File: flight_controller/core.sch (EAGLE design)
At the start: 115 parts, among them J1 M02, J10 M02, J11 M02, J12 M02, J13 M02, J14 M02, J15 M02, J16 M03, J17 M03, J18 M04, J19 M04, J2 M02, J20 M03, J21 M04, J3 M02, J4 M03, J5 M02, J6 M02, J7 M02, J8 M02, J9 M03, Q1 EM6K1, Q2 EM6K1, Q3 EM6K1, Q4 EM6K1, Q5 EM6K1, Q6 EM6K1, Q7 MOSFET-PCHANNEL-AON6407, U1 STM32F405, U2 MEAS-MS5611, U3 MPU-9250-QFN-24-NP, U4 MIC5219 3.3V, U5 USD-SOCKETNEW, Y1 16MHz

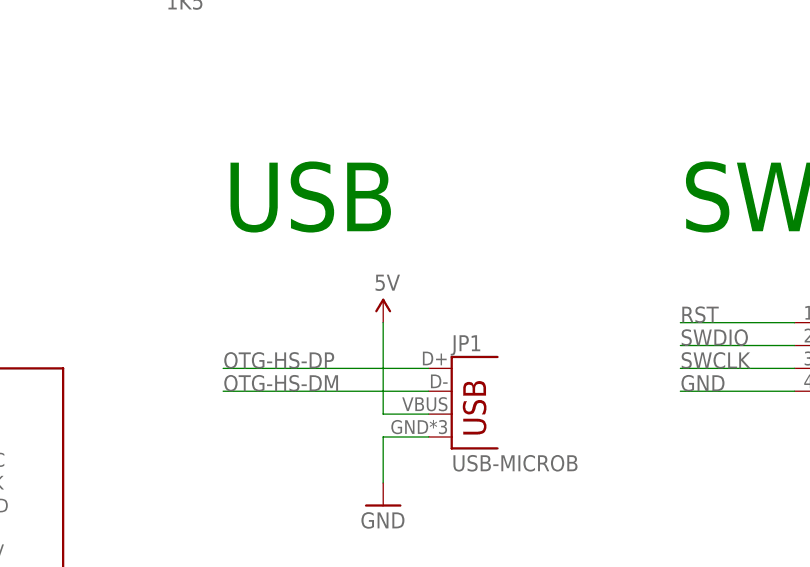
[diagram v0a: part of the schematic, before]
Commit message: Move USB 5V to VIN.
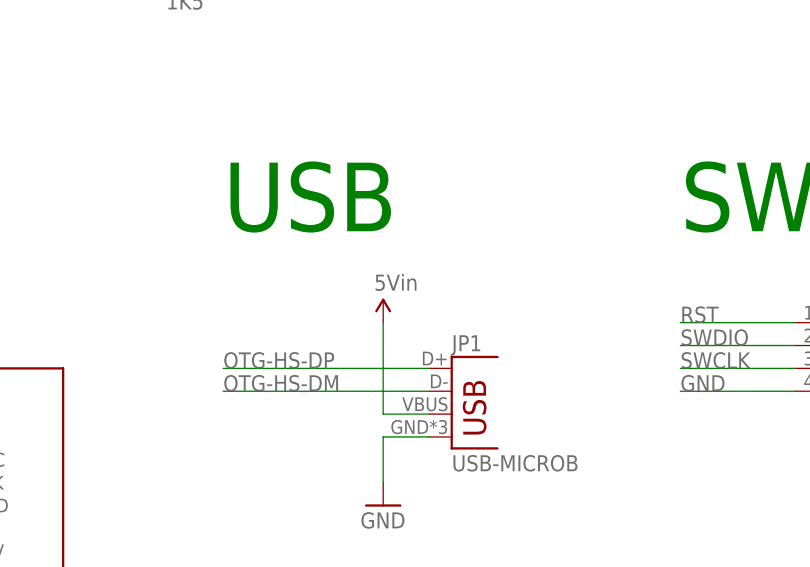
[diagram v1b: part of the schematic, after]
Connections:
- net 5V: no longer JP1.VBUS
- net VIN: now also JP1.VBUS
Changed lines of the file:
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@@
 <part name="JP1" library="SparkFun-Connectors" deviceset="USB" device="-MICROB"/>
 <part name="GND10" library="SparkFun-Aesthetics" deviceset="GND" device=""/>
-<part name="SUPPLY12" library="SparkFun-Aesthetics" deviceset="5V" device=""/>
 <part name="SUPPLY15" library="SparkFun-Aesthetics" deviceset="3.3V" device=""/>
 <part name="GND11" library="SparkFun-Aesthetics" deviceset="GND" device=""/>
@@
 <part name="J21" library="OSURC_Connectors" deviceset="M04" device=""/>
 <part name="J2" library="OSURC_Connectors" deviceset="M02" device=""/>
+<part name="SUPPLY1" library="SparkFun-Aesthetics" deviceset="VIN" device="" value="5Vin"/>
 </parts>
 <sheets>
@@
 <instance part="JP1" gate="G$1" x="106.68" y="-586.74"/>
 <instance part="GND10" gate="1" x="99.06" y="-594.36"/>
-<instance part="SUPPLY12" gate="G$1" x="99.06" y="-574.04"/>
 <instance part="SUPPLY15" gate="G$1" x="40.64" y="-574.04"/>
 <instance part="GND11" gate="1" x="40.64" y="-622.3"/>
@@
 <instance part="J21" gate="G$1" x="149.86" y="-579.12"/>
 <instance part="J2" gate="G$1" x="78.74" y="-416.56"/>
+<instance part="SUPPLY1" gate="G$1" x="99.06" y="-574.04"/>
 </instances>
 <busses>
@@
 <wire x1="139.7" y1="228.6" x2="132.08" y2="228.6" width="0.1524" layer="91"/>
 <label x="132.08" y="228.6" size="1.778" layer="95"/>
-</segment>
-<segment>
-<pinref part="JP1" gate="G$1" pin="VBUS"/>
-<wire x1="104.14" y1="-584.2" x2="99.06" y2="-584.2" width="0.1524" layer="91"/>
-<wire x1="99.06" y1="-584.2" x2="99.06" y2="-574.04" width="0.1524" layer="91"/>
-<pinref part="SUPPLY12" gate="G$1" pin="5V"/>
 </segment>
 <segment>
@@
 <pinref part="D1" gate="G$1" pin="2"/>
 </segment>
-</net>
+<segment>
+<pinref part="JP1" gate="G$1" pin="VBUS"/>
+<wire x1="104.14" y1="-584.2" x2="99.06" y2="-584.2" width="0.1524" layer="91"/>
+<wire x1="99.06" y1="-584.2" x2="99.06" y2="-574.04" width="0.1524" layer="91"/>
+<pinref part="SUPPLY1" gate="G$1" pin="VIN"/>
+</segment>
+</net>

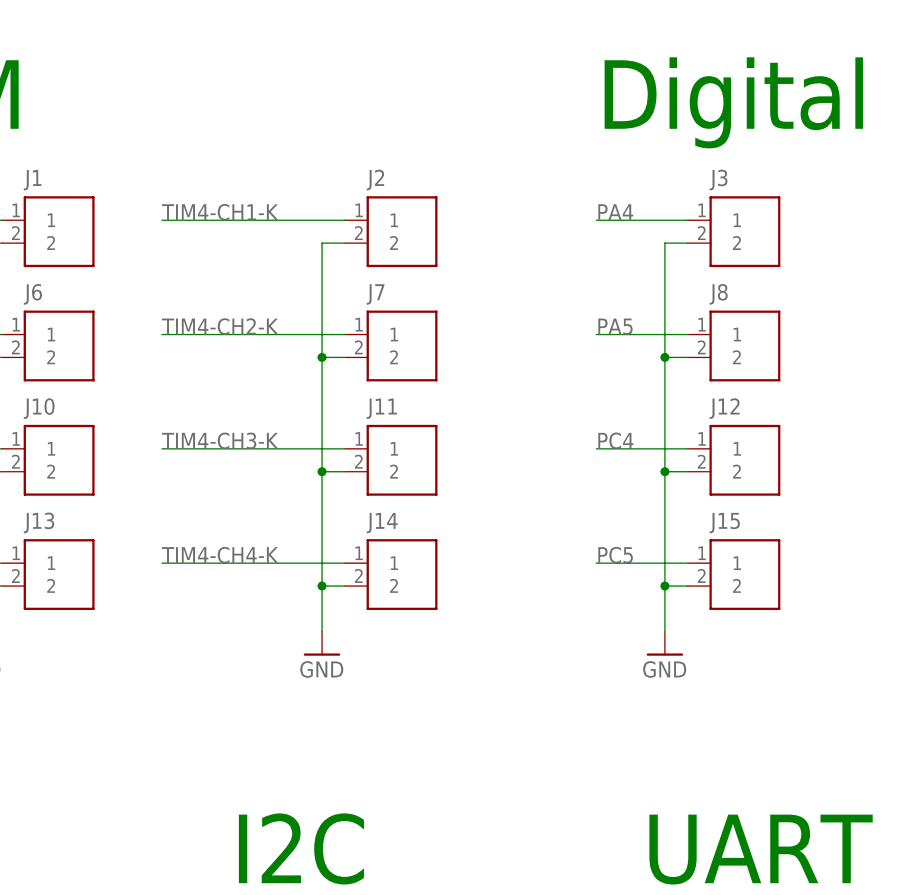
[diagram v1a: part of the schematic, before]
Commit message: Make last two PWM outputs 5V powered (for servos).
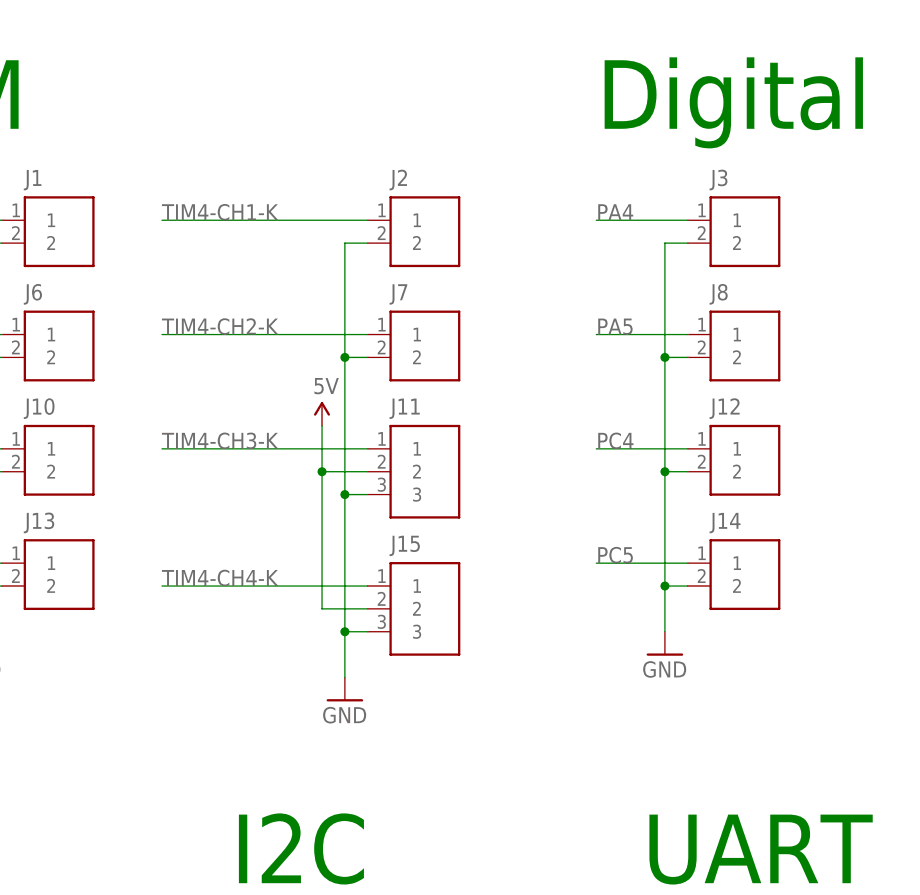
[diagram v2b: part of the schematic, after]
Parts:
- J11, J15: value M02 -> M03; device OSURC_Connectors:M02 -> OSURC_Connectors:M03
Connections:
- net 5V: now also J11.2, J15.2
- net GND: now also J11.3, J15.3; no longer J11.2, J15.2
- net PC5: now also J14.1; no longer J15.1
- net TIM4-CH4-K: now also J15.1; no longer J14.1
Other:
- moved on the sheet: J14, J2, J7
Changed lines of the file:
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@@
 <part name="J13" library="OSURC_Connectors" deviceset="M02" device=""/>
 <part name="J7" library="OSURC_Connectors" deviceset="M02" device=""/>
-<part name="J11" library="OSURC_Connectors" deviceset="M02" device=""/>
-<part name="J14" library="OSURC_Connectors" deviceset="M02" device=""/>
 <part name="J3" library="OSURC_Connectors" deviceset="M02" device=""/>
 <part name="J8" library="OSURC_Connectors" deviceset="M02" device=""/>
 <part name="J12" library="OSURC_Connectors" deviceset="M02" device=""/>
-<part name="J15" library="OSURC_Connectors" deviceset="M02" device=""/>
+<part name="J14" library="OSURC_Connectors" deviceset="M02" device=""/>
 <part name="J5" library="OSURC_Connectors" deviceset="M02" device=""/>
 <part name="J4" library="OSURC_Connectors" deviceset="M03" device=""/>
@@
 <part name="J2" library="OSURC_Connectors" deviceset="M02" device=""/>
 <part name="SUPPLY1" library="SparkFun-Aesthetics" deviceset="VIN" device="" value="5Vin"/>
+<part name="J11" library="OSURC_Connectors" deviceset="M03" device=""/>
+<part name="J15" library="OSURC_Connectors" deviceset="M03" device=""/>
+<part name="SUPPLY12" library="SparkFun-Aesthetics" deviceset="5V" device=""/>
 </parts>
 <sheets>
@@
 <instance part="SUPPLY4" gate="G$1" x="190.5" y="-414.02"/>
 <instance part="GND4" gate="1" x="33.02" y="-462.28"/>
-<instance part="GND5" gate="1" x="71.12" y="-462.28"/>
+<instance part="GND5" gate="1" x="73.66" y="-467.36"/>
 <instance part="GND7" gate="1" x="127" y="-528.32"/>
 <instance part="U5" gate="G$1" x="53.34" y="-594.36"/>
@@
 <instance part="J10" gate="G$1" x="40.64" y="-441.96"/>
 <instance part="J13" gate="G$1" x="40.64" y="-454.66"/>
-<instance part="J7" gate="G$1" x="78.74" y="-429.26"/>
-<instance part="J11" gate="G$1" x="78.74" y="-441.96"/>
-<instance part="J14" gate="G$1" x="78.74" y="-454.66"/>
+<instance part="J7" gate="G$1" x="81.28" y="-429.26"/>
 <instance part="J3" gate="G$1" x="116.84" y="-416.56"/>
 <instance part="J8" gate="G$1" x="116.84" y="-429.26"/>
 <instance part="J12" gate="G$1" x="116.84" y="-441.96"/>
-<instance part="J15" gate="G$1" x="116.84" y="-454.66"/>
+<instance part="J14" gate="G$1" x="116.84" y="-454.66"/>
 <instance part="J5" gate="G$1" x="358.14" y="-421.64"/>
 <instance part="J4" gate="G$1" x="200.66" y="-421.64"/>
@@
 <instance part="J19" gate="G$1" x="175.26" y="-508"/>
 <instance part="J21" gate="G$1" x="149.86" y="-579.12"/>
-<instance part="J2" gate="G$1" x="78.74" y="-416.56"/>
+<instance part="J2" gate="G$1" x="81.28" y="-416.56"/>
 <instance part="SUPPLY1" gate="G$1" x="99.06" y="-574.04"/>
+<instance part="J11" gate="G$1" x="81.28" y="-441.96"/>
+<instance part="J15" gate="G$1" x="81.28" y="-457.2"/>
+<instance part="SUPPLY12" gate="G$1" x="71.12" y="-436.88"/>
 </instances>
 <busses>
@@
 </segment>
 <segment>
-<wire x1="73.66" y1="-416.56" x2="71.12" y2="-416.56" width="0.1524" layer="91"/>
-<wire x1="73.66" y1="-454.66" x2="71.12" y2="-454.66" width="0.1524" layer="91"/>
-<wire x1="71.12" y1="-416.56" x2="71.12" y2="-429.26" width="0.1524" layer="91"/>
-<wire x1="71.12" y1="-429.26" x2="71.12" y2="-441.96" width="0.1524" layer="91"/>
-<wire x1="71.12" y1="-441.96" x2="71.12" y2="-454.66" width="0.1524" layer="91"/>
-<wire x1="73.66" y1="-429.26" x2="71.12" y2="-429.26" width="0.1524" layer="91"/>
-<junction x="71.12" y="-429.26"/>
-<wire x1="73.66" y1="-441.96" x2="71.12" y2="-441.96" width="0.1524" layer="91"/>
-<junction x="71.12" y="-441.96"/>
+<wire x1="76.2" y1="-416.56" x2="73.66" y2="-416.56" width="0.1524" layer="91"/>
+<wire x1="76.2" y1="-459.74" x2="73.66" y2="-459.74" width="0.1524" layer="91"/>
+<wire x1="73.66" y1="-416.56" x2="73.66" y2="-429.26" width="0.1524" layer="91"/>
+<wire x1="73.66" y1="-429.26" x2="73.66" y2="-444.5" width="0.1524" layer="91"/>
+<wire x1="73.66" y1="-444.5" x2="73.66" y2="-459.74" width="0.1524" layer="91"/>
+<wire x1="76.2" y1="-429.26" x2="73.66" y2="-429.26" width="0.1524" layer="91"/>
+<junction x="73.66" y="-429.26"/>
+<wire x1="76.2" y1="-444.5" x2="73.66" y2="-444.5" width="0.1524" layer="91"/>
+<junction x="73.66" y="-444.5"/>
 <pinref part="GND5" gate="1" pin="GND"/>
-<wire x1="71.12" y1="-454.66" x2="71.12" y2="-459.74" width="0.1524" layer="91"/>
-<junction x="71.12" y="-454.66"/>
+<wire x1="73.66" y1="-459.74" x2="73.66" y2="-464.82" width="0.1524" layer="91"/>
+<junction x="73.66" y="-459.74"/>
 <pinref part="J7" gate="G$1" pin="2"/>
-<pinref part="J11" gate="G$1" pin="2"/>
-<pinref part="J14" gate="G$1" pin="2"/>
 <pinref part="J2" gate="G$1" pin="2"/>
+<pinref part="J11" gate="G$1" pin="3"/>
+<pinref part="J15" gate="G$1" pin="3"/>
 </segment>
 <segment>
@@
 <pinref part="J8" gate="G$1" pin="2"/>
 <pinref part="J12" gate="G$1" pin="2"/>
-<pinref part="J15" gate="G$1" pin="2"/>
+<pinref part="J14" gate="G$1" pin="2"/>
 </segment>
 </net>
@@
 <pinref part="J4" gate="G$1" pin="2"/>
 <pinref part="J9" gate="G$1" pin="2"/>
+</segment>
+<segment>
+<pinref part="J11" gate="G$1" pin="2"/>
+<wire x1="76.2" y1="-441.96" x2="71.12" y2="-441.96" width="0.1524" layer="91"/>
+<wire x1="71.12" y1="-441.96" x2="71.12" y2="-436.88" width="0.1524" layer="91"/>
+<pinref part="J15" gate="G$1" pin="2"/>
+<wire x1="76.2" y1="-457.2" x2="71.12" y2="-457.2" width="0.1524" layer="91"/>
+<wire x1="71.12" y1="-457.2" x2="71.12" y2="-441.96" width="0.1524" layer="91"/>
+<junction x="71.12" y="-441.96"/>
+<pinref part="SUPPLY12" gate="G$1" pin="5V"/>
 </segment>
 </net>
@@
 <wire x1="111.76" y1="-452.12" x2="101.6" y2="-452.12" width="0.1524" layer="91"/>
 <label x="101.6" y="-452.12" size="1.778" layer="95"/>
-<pinref part="J15" gate="G$1" pin="1"/>
+<pinref part="J14" gate="G$1" pin="1"/>
 </segment>
 </net>
@@
 <net name="TIM4-CH1-K" class="0">
 <segment>
-<wire x1="73.66" y1="-414.02" x2="53.34" y2="-414.02" width="0.1524" layer="91"/>
+<wire x1="76.2" y1="-414.02" x2="53.34" y2="-414.02" width="0.1524" layer="91"/>
 <label x="53.34" y="-414.02" size="1.778" layer="95"/>
 <pinref part="J2" gate="G$1" pin="1"/>
@@
 <net name="TIM4-CH2-K" class="0">
 <segment>
-<wire x1="73.66" y1="-426.72" x2="53.34" y2="-426.72" width="0.1524" layer="91"/>
+<wire x1="76.2" y1="-426.72" x2="53.34" y2="-426.72" width="0.1524" layer="91"/>
 <label x="53.34" y="-426.72" size="1.778" layer="95"/>
 <pinref part="J7" gate="G$1" pin="1"/>
@@
 <net name="TIM4-CH3-K" class="0">
 <segment>
-<wire x1="73.66" y1="-439.42" x2="53.34" y2="-439.42" width="0.1524" layer="91"/>
+<wire x1="76.2" y1="-439.42" x2="53.34" y2="-439.42" width="0.1524" layer="91"/>
 <label x="53.34" y="-439.42" size="1.778" layer="95"/>
 <pinref part="J11" gate="G$1" pin="1"/>
@@
 <net name="TIM4-CH4-K" class="0">
 <segment>
-<wire x1="73.66" y1="-452.12" x2="53.34" y2="-452.12" width="0.1524" layer="91"/>
-<label x="53.34" y="-452.12" size="1.778" layer="95"/>
-<pinref part="J14" gate="G$1" pin="1"/>
-</segment>
-<segment>
+<wire x1="76.2" y1="-454.66" x2="53.34" y2="-454.66" width="0.1524" layer="91"/>
+<label x="53.34" y="-454.66" size="1.778" layer="95"/>
+<pinref part="J15" gate="G$1" pin="1"/>
+</segment>
+<segment>

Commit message: Component placement almost done, routing halfway done.
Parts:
- added S2, S3, S4, S5: STANDOFF_ELECTRICAL-#4, OSURC_Electromechanical:STANDOFF_ELECTRICAL-#4
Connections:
- net N$12 renamed STSB1+
- net N$15 renamed STSR2+
- net N$16 renamed STSG2+
- net N$19 renamed STSB2+
- net N$5 renamed STSB-
- net N$6 renamed STSG-
- net N$7 renamed STSR-
- net N$8 renamed STSR1+
- net N$9 renamed STSG1+
- removed net OTG-HS-ID: U1.GPIO.PB12
- net GND: now also S2.P$1, S3.P$1, S4.P$1, S5.P$1
- net USD-CD: now also U1.GPIO.PB12
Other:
- note added: "Standoffs"
- note added: "TODO: C15 unused"
- note removed: "TODO: B12 and C15 unused"
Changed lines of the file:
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@@
 <part name="J15" library="OSURC_Connectors" deviceset="M03" device=""/>
 <part name="SUPPLY12" library="SparkFun-Aesthetics" deviceset="5V" device=""/>
+<part name="S2" library="OSURC_Electromechanical" deviceset="STANDOFF_ELECTRICAL" device="-#4"/>
+<part name="S3" library="OSURC_Electromechanical" deviceset="STANDOFF_ELECTRICAL" device="-#4"/>
+<part name="S4" library="OSURC_Electromechanical" deviceset="STANDOFF_ELECTRICAL" device="-#4"/>
+<part name="S5" library="OSURC_Electromechanical" deviceset="STANDOFF_ELECTRICAL" device="-#4"/>
+<part name="GND6" library="SparkFun-Aesthetics" deviceset="GND" device=""/>
 </parts>
 <sheets>
@@
 <text x="33.02" y="-261.62" size="3.81" layer="91">VDDIO</text>
 <text x="101.6" y="-403.86" size="7.62" layer="91">Digital</text>
-<text x="15.24" y="152.4" size="1.778" layer="98">TODO: B12 and C15 unused</text>
+<text x="15.24" y="152.4" size="1.778" layer="98">TODO: C15 unused</text>
 <text x="15.24" y="-645.16" size="1.778" layer="98">TODO: pullups on data lines?</text>
 <text x="223.52" y="-403.86" size="7.62" layer="91">Test</text>
+<text x="347.98" y="-563.88" size="7.62" layer="91">Standoffs</text>
 </plain>
 <instances>
@@
 <instance part="J15" gate="G$1" x="81.28" y="-457.2"/>
 <instance part="SUPPLY12" gate="G$1" x="71.12" y="-436.88"/>
+<instance part="S2" gate="G$1" x="353.06" y="-576.58"/>
+<instance part="S3" gate="G$1" x="353.06" y="-591.82"/>
+<instance part="S4" gate="G$1" x="353.06" y="-607.06"/>
+<instance part="S5" gate="G$1" x="353.06" y="-622.3"/>
+<instance part="GND6" gate="1" x="363.22" y="-629.92"/>
 </instances>
 <busses>
@@
 <pinref part="J12" gate="G$1" pin="2"/>
 <pinref part="J14" gate="G$1" pin="2"/>
+</segment>
+<segment>
+<pinref part="S2" gate="G$1" pin="P$1"/>
+<wire x1="360.68" y1="-576.58" x2="363.22" y2="-576.58" width="0.1524" layer="91"/>
+<wire x1="363.22" y1="-576.58" x2="363.22" y2="-591.82" width="0.1524" layer="91"/>
+<pinref part="S3" gate="G$1" pin="P$1"/>
+<wire x1="363.22" y1="-591.82" x2="363.22" y2="-607.06" width="0.1524" layer="91"/>
+<wire x1="363.22" y1="-607.06" x2="363.22" y2="-622.3" width="0.1524" layer="91"/>
+<wire x1="363.22" y1="-622.3" x2="363.22" y2="-627.38" width="0.1524" layer="91"/>
+<wire x1="360.68" y1="-591.82" x2="363.22" y2="-591.82" width="0.1524" layer="91"/>
+<pinref part="S4" gate="G$1" pin="P$1"/>
+<wire x1="360.68" y1="-607.06" x2="363.22" y2="-607.06" width="0.1524" layer="91"/>
+<pinref part="S5" gate="G$1" pin="P$1"/>
+<wire x1="360.68" y1="-622.3" x2="363.22" y2="-622.3" width="0.1524" layer="91"/>
+<pinref part="GND6" gate="1" pin="GND"/>
+<junction x="363.22" y="-591.82"/>
+<junction x="363.22" y="-607.06"/>
+<junction x="363.22" y="-622.3"/>
 </segment>
 </net>
@@
 </segment>
 </net>
-<net name="OTG-HS-ID" class="0">
-<segment>
-<wire x1="53.34" y1="170.18" x2="30.48" y2="170.18" width="0.1524" layer="91"/>
-<label x="30.48" y="170.18" size="1.778" layer="95"/>
-<pinref part="U1" gate=".GPIO" pin="PB12"/>
-</segment>
-</net>
 <net name="OTG-HS-DM" class="0">
 <segment>
@@
 <junction x="38.1" y="-612.14"/>
 </segment>
+<segment>
+<wire x1="53.34" y1="170.18" x2="30.48" y2="170.18" width="0.1524" layer="91"/>
+<label x="30.48" y="170.18" size="1.778" layer="95"/>
+<pinref part="U1" gate=".GPIO" pin="PB12"/>
+</segment>
 </net>
 <net name="SPISS-UNUSED" class="0">
@@
 </segment>
 </net>
-<net name="N$5" class="0">
+<net name="STSB-" class="0">
 <segment>
 <pinref part="LED8" gate="G$1" pin="B-"/>
@@
 </segment>
 </net>
-<net name="N$6" class="0">
+<net name="STSG-" class="0">
 <segment>
 <pinref part="LED8" gate="G$1" pin="G-"/>
@@
 </segment>
 </net>
-<net name="N$7" class="0">
+<net name="STSR-" class="0">
 <segment>
 <pinref part="LED8" gate="G$1" pin="R-"/>
@@
 </segment>
 </net>
-<net name="N$8" class="0">
+<net name="STSR1+" class="0">
 <segment>
 <pinref part="LED5" gate="G$1" pin="R+"/>
@@
 </segment>
 </net>
-<net name="N$9" class="0">
+<net name="STSG1+" class="0">
 <segment>
 <pinref part="LED5" gate="G$1" pin="G+"/>
@@
 </segment>
 </net>
-<net name="N$12" class="0">
+<net name="STSB1+" class="0">
 <segment>
 <pinref part="LED5" gate="G$1" pin="B+"/>
@@
 </segment>
 </net>
-<net name="N$15" class="0">
+<net name="STSR2+" class="0">
 <segment>
 <pinref part="LED8" gate="G$1" pin="R+"/>
@@
 </segment>
 </net>
-<net name="N$16" class="0">
+<net name="STSG2+" class="0">
 <segment>
 <pinref part="LED8" gate="G$1" pin="G+"/>
@@
 </segment>
 </net>
-<net name="N$19" class="0">
+<net name="STSB2+" class="0">
 <segment>
 <pinref part="LED8" gate="G$1" pin="B+"/>

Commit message: More layout, and replace passives with OSURC's own.
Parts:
- C1, C2: device SparkFun-Capacitors:18PF-50V-5%(0603) -> OSURC_Passives:CAP-18PF-50V-5%(0603)
- C10, C13, C14, C15, C17, C6, C7, C8, C9: value 0.1uF -> 100nF; device SparkFun-Capacitors:0.1UF-25V-5%(0603) -> OSURC_Passives:CAP-100NF-16V-10%(0603)
- C11, C12: device SparkFun-Capacitors:2.2UF-10V-20%(0603) -> OSURC_Passives:CAP-2.2UF-10V-10%(0603)
- C16: device SparkFun-Capacitors:10NF/10000PF-50V-10%(0603) -> OSURC_Passives:CAP-10NF-50V-10%(0603)
- C3, C4: device SparkFun-Capacitors:10UF-16V-10%(TANT) -> OSURC_Passives:CAP-10UF-10V-10%(0805)
- C5: device SparkFun-Capacitors:1NF/1000PF-50V-10%(0603) -> OSURC_Passives:CAP-1NF-50V-10%(0603)
- R1, R10, R12, R17, R2, R23, R24: device SparkFun-Passives:RESISTOR0603-RES -> OSURC_Passives:RES-680OHM-0.1W-5%(0603)
- R11, R13, R16, R18: device SparkFun-Passives:RESISTOR0603-RES -> OSURC_Passives:RES-100OHM-0.1W-5%(0603)
- R14, R8: device SparkFun-Passives:RESISTOR0603-RES -> OSURC_Passives:RES-120OHM-0.1W-5%(0603)
- R15: device SparkFun-Passives:RESISTOR0603-RES -> OSURC_Passives:RES-165OHM-0.1W-1%(0603)
- R19, R20, R21, R22, R3, R4, R5, R6, R7: value 1K -> 1k; device SparkFun:RESISTOR0603-RES -> OSURC_Passives:RES-1KOHM-0.1W-5%(0603)
- R25: value 20K -> 20k; device SparkFun:RESISTOR0603-RES -> OSURC_Passives:RES-20KOHM-0.1W-1%(0603)
- R26, R27, R28, R29: value 20K -> 20k; device SparkFun-Passives:RESISTOR0603-RES -> OSURC_Passives:RES-20KOHM-0.1W-0.1%(0603)
- R30, R32: value 20K -> 20k; device SparkFun-Passives:RESISTOR0603-RES -> OSURC_Passives:RES-20KOHM-0.1W-1%(0603)
- R31, R33: value 1K5 -> 1.5k; device SparkFun-Passives:RESISTOR0603-RES -> OSURC_Passives:RES-1.5KOHM-0.1W-5%(0603)
- R34: value 1K -> 1k; device SparkFun-Passives:RESISTOR0603-RES -> OSURC_Passives:RES-1KOHM-0.1W-5%(0603)
- R9: value 1K1 -> 1.1k; device SparkFun-Passives:RESISTOR0603-RES -> OSURC_Passives:RES-1.1KOHM-0.1W-5%(0603)
- S1: value SWITCH-MOMENTARY-2SMD -> SWITCH-MOMENTARY-2-PTS525; device SparkFun-Electromechanical:SWITCH-MOMENTARY-2SMD -> OSURC_Electromechanical:SWITCH-MOMENTARY-2-PTS525
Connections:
- net 3.3V: now also C10.2, C13.2, C14.2, C15.2, C16.2, C4.2, C6.2, C8.2, C9.2; no longer C10.1, C13.1, C14.1, C15.1, C16.1, C4.+, C6.1, C8.1, C9.1
- net 5V: now also C3.2; no longer C3.+
- net F4-VCAP-1: now also C11.2; no longer C11.1
- net F4-VCAP-2: now also C12.2; no longer C12.1
- net GND: now also C1.1, C10.1, C11.1, C12.1, C13.1, C14.1, C15.1, C16.1, C17.1, C2.1, C3.1, C4.1, C5.1, C6.1, C8.1, C9.1; no longer C1.2, C10.2, C11.2, C12.2, C13.2, C14.2, C15.2, C16.2, C17.2, C2.2, C3.-, C4.-, C5.2, C6.2, C8.2, C9.2
- net MIC-BP: now also C5.2; no longer C5.1
- net MPU9250-REGOUT: now also C17.2; no longer C17.1
- net OSC-IN: now also C1.2; no longer C1.1
- net OSC-OUT: now also C2.2; no longer C2.1
